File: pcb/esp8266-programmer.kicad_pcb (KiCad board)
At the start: 2 copper layers, 19 parts, among them P1 USB_OTG, P2 CONN_01X04, P3 CONN_02X05, SW1 RESET, SW2 FLASH, SW3 SW_DP3T, U1 MCP1700T-3302E/TT, U2 MCP2221-I/SL, U99 ESP-12

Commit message: Interim stage - Part 2
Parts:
- moved JP1 15.8 mm to (110.5, 116.5), turned to 0 degrees
- moved SW2 14.9 mm to (96.0, 104.5)
- moved P1 13.9 mm to (95.0, 119.5)
- moved P2 13.8 mm to (108.0, 121.5)
- moved U1 9.96 mm to (91.5, 114.5)
- moved U2 9.63 mm to (85.0, 118.0), turned to 0 degrees
- moved C2 9.09 mm to (115.5, 110.5), turned to 90 degrees
- moved C1 8.82 mm to (109.0, 110.5)
- moved R1 7.19 mm to (103.0, 104.0), turned to 180 degrees
- moved R4 6.97 mm to (124.0, 104.0), turned to 180 degrees
- moved C4 6.77 mm to (97.5, 114.0), turned to 180 degrees
- moved R2 5.51 mm to (110.0, 104.0), turned to 180 degrees
- moved R3 5.41 mm to (117.0, 104.0), turned to 180 degrees
- moved SW1 2.18 mm to (87.5, 104.5)
- moved SW3 1.36 mm to (117.5, 122.0)

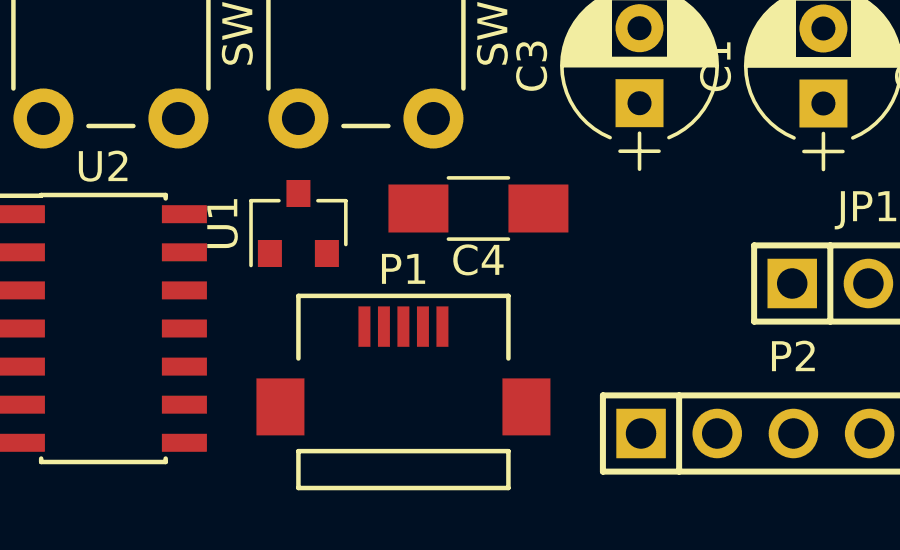
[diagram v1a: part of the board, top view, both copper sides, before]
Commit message: Add CH340G and new reset/flash circuit
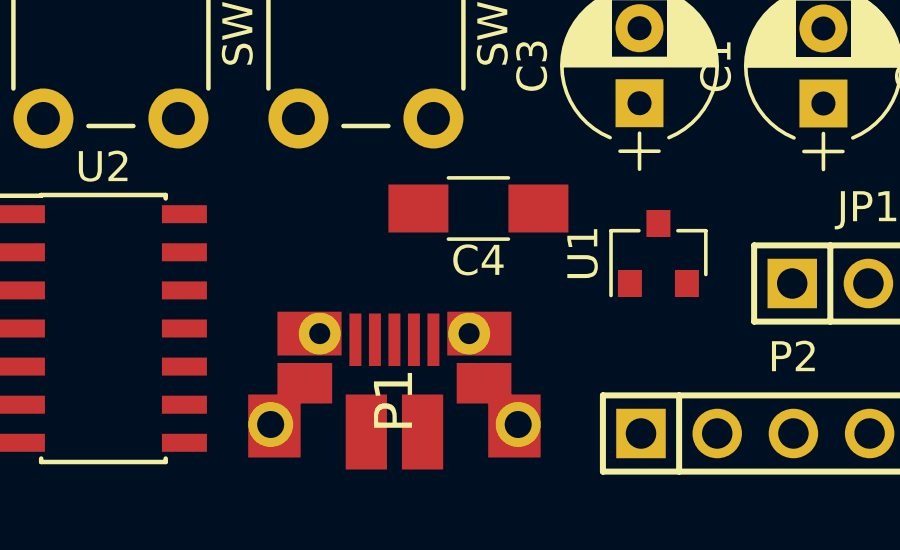
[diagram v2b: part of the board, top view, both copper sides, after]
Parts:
- P1: footprint ruriwo/KiCad_MicroUSB.pretty:ZX62R-B-5P -> greatscottgadgets/gsg-kicad-lib/gsg-modules.pretty:USB-MICROB-FCI-10103592
- moved U1 12.0 mm to (103.5, 115.5)
- moved P1 3.41 mm to (94.7, 122.9), turned to 90 degrees
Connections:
- C3 pad 1: VBUS -> VCC
- JP1 pad 3: Net-(JP1-Pad3) -> (no net)
- P1 pad 4: Net-(P1-Pad4) -> (no net)
- P2 pad 3: Net-(P2-Pad3) -> (no net)
- SW3 pad 4: Net-(SW3-Pad4) -> (no net)
- U1 pad 2: Net-(SW3-Pad7) -> (no net)
- U2 pad 1: VBUS -> VCC
- U2 pad 10: Net-(U2-Pad10) -> (no net)
- U2 pad 2: Net-(U2-Pad2) -> (no net)
- U2 pad 3: Net-(U2-Pad3) -> (no net)
- U2 pad 4: Net-(U2-Pad4) -> (no net)
- U2 pad 7: Net-(U2-Pad7) -> (no net)
- U2 pad 8: Net-(U2-Pad8) -> (no net)
- U2 pad 9: Net-(U2-Pad9) -> (no net)
